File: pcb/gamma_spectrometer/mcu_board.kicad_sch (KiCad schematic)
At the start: 39 parts, among them U301 TL431, U302 STM32G474MET6, U303 W25Q64JVSSIQ, Y301 ABM8G-16.000MHZ-4Y-T3

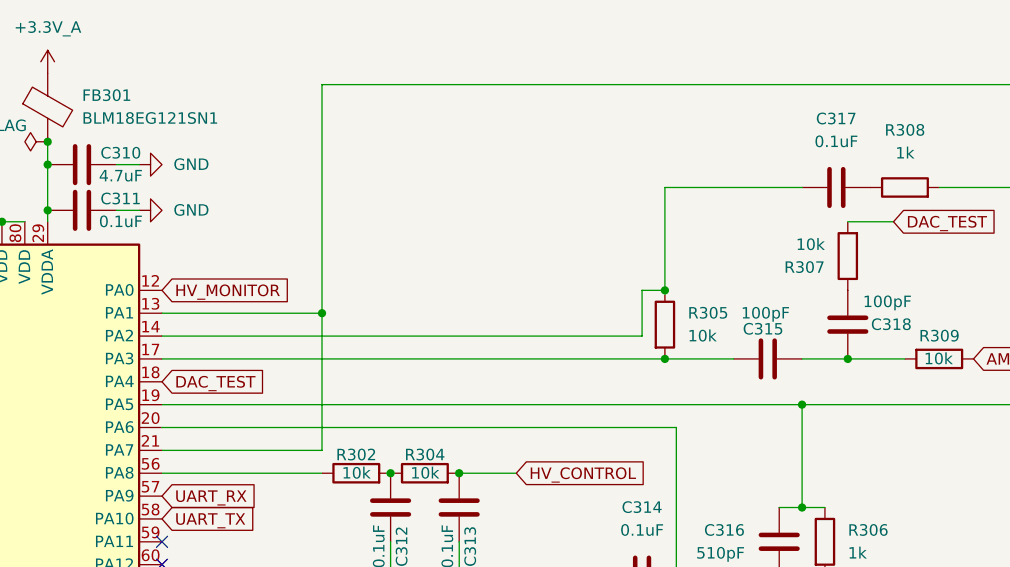
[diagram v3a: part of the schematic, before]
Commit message: pcb: схема MCU + BOM — R314 (R_pz 10k) добавлен пользователем (источник нетлиста)
Согласует репо с уже закоммиченным нетлистом (фикс C2). Схему правил пользователь.

Co-Authored-By: Claude Opus 4.8 <noreply@anthropic.com>
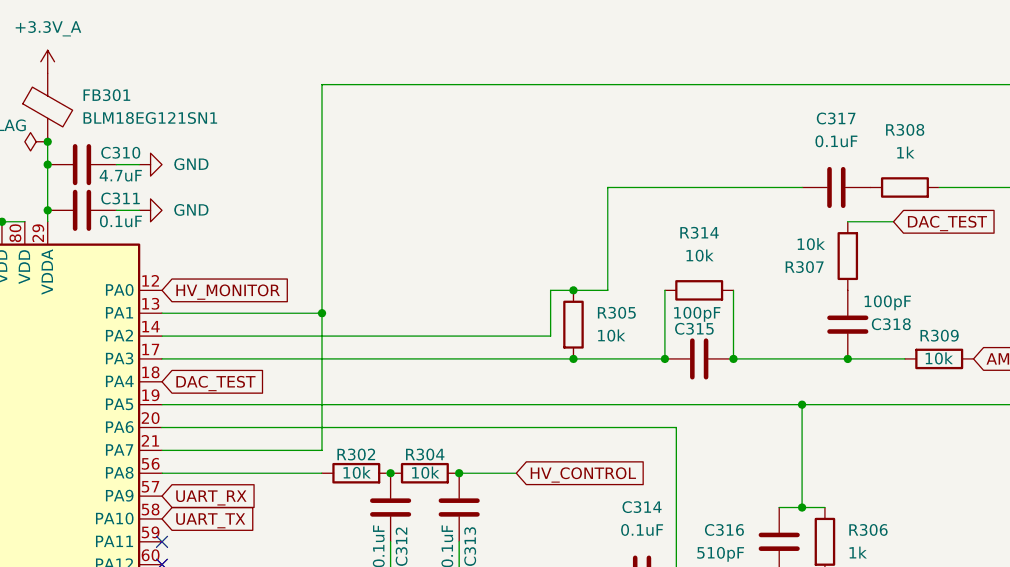
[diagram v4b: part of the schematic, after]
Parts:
- added R314: 10k, Resistor_SMD:R_0603_1608Metric_Pad0.98x0.95mm_HandSolder, symbol Device:R
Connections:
- net at C315.1, C318.1, R309.2: now also R314.2
- net at C315.2, R305.2, U302.17 (PA3): now also R314.1
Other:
- moved on the sheet: C315, R305
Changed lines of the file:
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@@
 	)
 	(junction
-		(at 396.24 173.99)
+		(at 351.79 138.43)
 		(diameter 0)
 		(color 0 0 0 0)
 	)
 	(junction
-		(at 200.66 130.81)
+		(at 396.24 173.99)
 		(diameter 0)
 		(color 0 0 0 0)
 	)
 	(junction
-		(at 344.17 130.81)
+		(at 200.66 130.81)
 		(diameter 0)
 		(color 0 0 0 0)
@@
 	)
 	(junction
+		(at 344.17 138.43)
+		(diameter 0)
+		(color 0 0 0 0)
+	)
+	(junction
 		(at 213.36 130.81)
 		(diameter 0)
@@
 	)
 	(junction
-		(at 344.17 138.43)
+		(at 334.01 138.43)
 		(diameter 0)
 		(color 0 0 0 0)
@@
 	)
 	(junction
+		(at 334.01 130.81)
+		(diameter 0)
+		(color 0 0 0 0)
+	)
+	(junction
 		(at 345.44 162.56)
 		(diameter 0)
@@
 	(wire
 		(pts
-			(xy 344.17 119.38) (xy 344.17 130.81)
+			(xy 337.82 119.38) (xy 337.82 130.81)
 		)
 		(stroke
@@
 	(wire
 		(pts
-			(xy 359.41 138.43) (xy 364.49 138.43)
+			(xy 351.79 138.43) (xy 364.49 138.43)
 		)
 		(stroke
@@
 	(wire
 		(pts
+			(xy 344.17 130.81) (xy 344.17 138.43)
+		)
+		(stroke
+			(width 0)
+			(type default)
+		)
+	)
+	(wire
+		(pts
 			(xy 200.66 128.27) (xy 200.66 130.81)
 		)
@@
 	(wire
 		(pts
+			(xy 334.01 130.81) (xy 337.82 130.81)
+		)
+		(stroke
+			(width 0)
+			(type default)
+		)
+	)
+	(wire
+		(pts
 			(xy 262.89 123.19) (xy 265.43 123.19)
 		)
@@
 	(wire
 		(pts
-			(xy 341.63 135.89) (xy 341.63 130.81)
+			(xy 331.47 135.89) (xy 331.47 130.81)
 		)
 		(stroke
@@
 	(wire
 		(pts
-			(xy 359.41 119.38) (xy 344.17 119.38)
+			(xy 359.41 119.38) (xy 337.82 119.38)
 		)
 		(stroke
@@
 	(wire
 		(pts
+			(xy 351.79 130.81) (xy 351.79 138.43)
+		)
+		(stroke
+			(width 0)
+			(type default)
+		)
+	)
+	(wire
+		(pts
 			(xy 260.35 123.19) (xy 262.89 123.19)
 		)
@@
 	(wire
 		(pts
-			(xy 306.07 148.59) (xy 288.29 148.59)
+			(xy 334.01 138.43) (xy 344.17 138.43)
 		)
 		(stroke
@@
 	(wire
 		(pts
-			(xy 341.63 130.81) (xy 344.17 130.81)
+			(xy 306.07 148.59) (xy 288.29 148.59)
 		)
 		(stroke
@@
 	(wire
 		(pts
-			(xy 265.43 120.65) (xy 265.43 123.19)
+			(xy 331.47 130.81) (xy 334.01 130.81)
 		)
 		(stroke
@@
 	(wire
 		(pts
-			(xy 359.41 143.51) (xy 359.41 154.94)
+			(xy 265.43 120.65) (xy 265.43 123.19)
 		)
 		(stroke
@@
 	(wire
 		(pts
-			(xy 288.29 138.43) (xy 344.17 138.43)
+			(xy 359.41 143.51) (xy 359.41 154.94)
 		)
 		(stroke
@@
 	(wire
 		(pts
-			(xy 288.29 135.89) (xy 341.63 135.89)
+			(xy 288.29 138.43) (xy 334.01 138.43)
 		)
 		(stroke
@@
 	(wire
 		(pts
-			(xy 321.31 151.13) (xy 327.66 151.13)
+			(xy 288.29 135.89) (xy 331.47 135.89)
 		)
 		(stroke
@@
 	(wire
 		(pts
-			(xy 401.32 66.04) (xy 396.24 66.04)
+			(xy 321.31 151.13) (xy 327.66 151.13)
 		)
 		(stroke
@@
 	(wire
 		(pts
-			(xy 247.65 143.51) (xy 243.84 143.51)
+			(xy 401.32 66.04) (xy 396.24 66.04)
 		)
 		(stroke
@@
 	(wire
 		(pts
-			(xy 344.17 138.43) (xy 351.79 138.43)
+			(xy 247.65 143.51) (xy 243.84 143.51)
 		)
 		(stroke
@@
 	(symbol
 		(lib_id "Device:C")
-		(at 355.6 138.43 270)
+		(at 347.98 138.43 270)
 		(unit 1)
 		(exclude_from_sim no)
@@
 		(dnp no)
 		(property "Reference" "C315"
-			(at 355.092 135.128 90)
+			(at 347.472 135.128 90)
 			(effects
 				(font
@@
 		)
 		(property "Value" "100pF"
-			(at 355.346 133.35 90)
+			(at 347.726 133.35 90)
 			(effects
 				(font
@@
 		)
 		(property "Footprint" "Capacitor_SMD:C_0603_1608Metric_Pad1.08x0.95mm_HandSolder"
-			(at 351.79 139.3952 0)
+			(at 344.17 139.3952 0)
 			(effects
 				(font
@@
 		)
 		(property "Datasheet" "~"
-			(at 355.6 138.43 0)
+			(at 347.98 138.43 0)
 			(effects
 				(font
@@
 		)
 		(property "Description" "Unpolarized capacitor"
-			(at 355.6 138.43 0)
+			(at 347.98 138.43 0)
 			(effects
 				(font
@@
 		)
 		(property "KLC_S3.3" ""
-			(at 355.6 138.43 90)
+			(at 347.98 138.43 90)
 			(effects
 				(font
@@
 		)
 		(property "KLC_S4.1" ""
-			(at 355.6 138.43 90)
+			(at 347.98 138.43 90)
 			(effects
 				(font
@@
 		)
 		(property "PN" "CC0603JRNPO9BN101"
-			(at 355.6 138.43 90)
+			(at 347.98 138.43 90)
 			(effects
 				(font
@@
 		)
 		(property "Ссылка на покупку " "https://www.electronshik.ru/item/YAG/CC0603JRNPO9BN101"
-			(at 355.6 138.43 90)
+			(at 347.98 138.43 90)
 			(effects
 				(font
@@
 	)
 	(symbol
+		(lib_id "Device:R")
+		(at 347.98 130.81 90)
+		(unit 1)
+		(exclude_from_sim no)
+		(in_bom yes)
+		(on_board yes)
+		(dnp no)
+		(fields_autoplaced yes)
+		(property "Reference" "R314"
+			(at 347.98 124.46 90)
+			(effects
+				(font
+					(size 1.27 1.27)
+				)
+			)
+		)
+		(property "Value" "10k"
+			(at 347.98 127 90)
+			(effects
+				(font
+					(size 1.27 1.27)
+				)
+			)
+		)
+		(property "Footprint" "Resistor_SMD:R_0603_1608Metric_Pad0.98x0.95mm_HandSolder"
+			(at 347.98 132.588 90)
+			(effects
+				(font
+					(size 1.27 1.27)
+				)
+				(hide yes)
+			)
+		)
+		(property "Datasheet" "~"
+			(at 347.98 130.81 0)
+			(effects
+				(font
+					(size 1.27 1.27)
+				)
+				(hide yes)
+			)
+		)
+		(property "Description" "Resistor"
+			(at 347.98 130.81 0)
+			(effects
+				(font
+					(size 1.27 1.27)
+				)
+				(hide yes)
+			)
+		)
+		(property "PN" "RC0603FR-0710KL"
+			(at 347.98 130.81 90)
+			(effects
+				(font
+					(size 1.27 1.27)
+				)
+				(hide yes)
+			)
+		)
+		(property "Ссылка на покупку " "https://www.electronshik.ru/item/YAG/RC0603FR-0710KL"
+			(at 347.98 130.81 90)
+			(effects
+				(font
+					(size 1.27 1.27)
+				)
+				(hide yes)
+			)
+		)
+		(pin "1"
+		)
+		(pin "2"
+		)
+		(instances
+			(project ""
+				(path "/9de23c55-b97f-4e07-9aa5-29ce30f3c480/0e491218-e2a9-4640-b27e-9c4e6f92e006"
+					(reference "R314")
+					(unit 1)
+				)
+			)
+		)
+	)
+	(symbol
 		(lib_id "power:GND")
 		(at 402.59 115.57 0)
@@
 	(symbol
 		(lib_id "Device:R")
-		(at 344.17 134.62 0)
+		(at 334.01 134.62 0)
 		(unit 1)
 		(exclude_from_sim no)
@@
 		(fields_autoplaced yes)
 		(property "Reference" "R305"
-			(at 346.71 133.3499 0)
+			(at 336.55 133.3499 0)
 			(effects
 				(font
@@
 		)
 		(property "Value" "10k"
-			(at 346.71 135.8899 0)
+			(at 336.55 135.8899 0)
 			(effects
 				(font
@@
 		)
 		(property "Footprint" "Resistor_SMD:R_0603_1608Metric_Pad0.98x0.95mm_HandSolder"
-			(at 342.392 134.62 90)
+			(at 332.232 134.62 90)
 			(effects
 				(font
@@
 		)
 		(property "Datasheet" "~"
-			(at 344.17 134.62 0)
+			(at 334.01 134.62 0)
 			(effects
 				(font
@@
 		)
 		(property "Description" "Resistor"
-			(at 344.17 134.62 0)
+			(at 334.01 134.62 0)
 			(effects
 				(font
@@
 		)
 		(property "KLC_S3.3" ""
-			(at 344.17 134.62 0)
+			(at 334.01 134.62 0)
 			(effects
 				(font
@@
 		)
 		(property "KLC_S4.1" ""
-			(at 344.17 134.62 0)
+			(at 334.01 134.62 0)
 			(effects
 				(font
@@
 		)
 		(property "PN" "RC0603FR-0710KL"
-			(at 344.17 134.62 0)
+			(at 334.01 134.62 0)
 			(effects
 				(font
@@
 		)
 		(property "Ссылка на покупку " "https://www.electronshik.ru/item/YAG/RC0603FR-0710KL"
-			(at 344.17 134.62 0)
+			(at 334.01 134.62 0)
 			(effects
 				(font

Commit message: fix: полярность тракта, опора REF35250, DRC по электрике в ноль
ПОЛЯРНОСТЬ (главное). Анод ФЭУ забирает условный ток => выход TIA идёт
вверх => импульс на АЦП положительный. В доках и прошивке была обратная
конвенция, выросшая из sim2_shaper.cir, где источник тока анода развёрнут
(`I_pmt 0 anode` вместо `I_pmt anode 0`); sim_divider_complete.cir всё это
время делал верно — две деки противоречили друг другу.

Последствия при старых смещениях (sim_polarity_headroom.cir, реальная
модель ADA4817): OPAMP1 уходил вниз до -1.09 В при VOLSAT 100 мВ (клиппинг
с ~1.2 МэВ), АЦП вверх до 3.99 В при VREF+ 2.495 (обрезка с ~0.70 МэВ).
Прибор мерил бы до 700 кэВ вместо 3.5 МэВ.

Исправление — два резистора, железо не переделывается:
  R313 2.0к -> 14.7к   V_A 0.490 -> 1.602 В
  R311 5.9к -> 909     V_PB0 0.529 -> 0.099 В, базовая линия АЦП -> 0.408 В
Запасы на потолке 3.5 МэВ (sim_bias_fixed.cir): OPAMP1 0.575..2.515,
OPAMP2 1.580..2.082, АЦП 0.308..2.276 (до VREF+ +0.224 В).
Попутно вскрыто: выход OPAMP1 сидит на 1.5*V_A, а не на V_A — R314 (фикс C2)
создаёт путь по постоянному току в обход C315. Нигде не было записано.
В прошивке остаётся сделать `amplitude = sample - baseline`.

ОПОРА. TL431DBZ -> REF35250QDBVR (SOT-23-6) по итогам ревью инженера:
параметрический шунт заменён последовательной опорой. 12 ppm/°C вместо 50
(у клона YOUTAI до 300), точность ±0.05%. Дрейф калибровки на ±30 °C:
0.9% -> 0.036%. R301 удалён, C303 100нФ -> 1мкФ (обязательный выходной),
добавлен C322 1мкФ на вывод NR. Правило шпаргалки №9 (ток шунта) для U301
больше не применимо; U202 на ВВ-плате остаётся TL431.
⚠ REF35205, который он назвал — это 2.048 В, не подходит (пик 2.118 В).

DRC. По электрике ноль нарушений: clearance, track_dangling, via_dangling,
holes_co_located, starved_thermal — все пусты. Всего 774 -> 402, остаток
целиком шелкография и courtyard.
- 25 GND-падов переведены на сплошное соединение с зоной (стойки, развязка,
  кварц, земля MAX1847, выход опоры)
- экран USB-C заземлён: J101 пер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
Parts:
- removed R301: R330, Resistor_SMD:R_0603_1608Metric_Pad0.98x0.95mm_HandSolder, symbol Device:R
- removed U301: TL431, Package_TO_SOT_SMD:SOT-23, symbol Reference_Voltage:TL431DBZ
- added C322: 1uF, Capacitor_SMD:C_0805_2012Metric_Pad1.18x1.45mm_HandSolder, symbol Device:C
- added U301: REF35250QDBVR, Package_TO_SOT_SMD:SOT-23-6, symbol Reference_Voltage:REF35250QDBVR
- C303: value 0.1uF -> 1uF; footprint Capacitor_SMD:C_0603_1608Metric_Pad1.08x0.95mm_HandSolder -> Capacitor_SMD:C_0805_2012Metric_Pad1.18x1.45mm_HandSolder; PN CC0603JRX7R9BB104 -> CC0805JKX7R9BB105; Ссылка на покупку  https://www.electronshik.ru/item/YAG/CC0603JRX7R9BB104 -> https://www.electronshik.ru/item/YAG/CC0805JKX7R9BB105
- R311: value 5.9k -> 909R; PN RC0603FR-075K9L -> RC0603FR-07909RL; Ссылка на покупку  https://www.electronshik.ru/item/YAG/RC0603FR-075K9L -> https://www.electronshik.ru/item/YAG/RC0603FR-07909RL
- R313: value 2k -> 14.7k; PN RC0603FR-072KL -> RC0603FR-0714K7L; Ссылка на покупку  https://www.electronshik.ru/item/YAG/RC0603FR-072KL -> https://www.electronshik.ru/item/YAG/RC0603FR-0714K7L
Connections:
- net +3.3V_A: now also U301.3 (EN), U301.4 (VIN)
- net GND: now also C322.2, U301.1 (GND), U301.2 (GND)
- net at C303.2, R303.1, R310.1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: now also U301.6 (VREF)
- new net: C322.1, U301.5 (NR)

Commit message: pcb: земля МК подключена, C320 удалён, C314/C317 → 1 мкФ, SWD-пятаки убраны
Плата МК:
- все GND-выводы U302 подключены (15, 27/VSSA, 40, 50 висели);
  зона GND на F.Cu: зазор 0.5 → 0.25 мм, зазор термобарьера → 0.2 мм;
  GND-виа 41 → 97. Остаётся: выводы 50 и 61 на одной спице (starved_thermal).
- TP_SWD301 удалён: прошивка — проводами к выводам 63/64/7 U302.

Схема МК (ревью REVIEW_critic_2026-09-15, находки 1.1 и 1.3, вариант V2):
- C320 удалён (100 нФ на PB0 делил сигнал ×0.5 вместе с C314);
- C314, C317: 100 нФ → 1 мкФ (CC0603JRX7R7BB105), τ связей ~1 мс.

USB-плата: J101 на проектной копии футпринта USB-C (экран на GND).

Co-Authored-By: Claude Opus 5 (1M context) <noreply@anthropic.com>
Claude-Session: https://claude.ai/code/session_018uEKxzknn1WsQbGcTkkQF5
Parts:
- removed C320: 0.1uF, Capacitor_SMD:C_0603_1608Metric_Pad1.08x0.95mm_HandSolder, symbol Device:C
- C314, C317: value 0.1uF -> 1uF; PN CC0603JRX7R9BB104 -> CC0603JRX7R7BB105; Ссылка на покупку  https://www.electronshik.ru/item/YAG/CC0603JRX7R9BB104 -> https://www.electronshik.ru/item/YAG/CC0603JRX7R7BB105
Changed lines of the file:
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@@
 			)
 		)
-		(property "Value" "0.1uF"
+		(property "Value" "1uF"
 			(at 341.63 157.48 90)
 			(effects
@@
 			)
 		)
-		(property "PN" "CC0603JRX7R9BB104"
+		(property "PN" " CC0603JRX7R7BB105"
 			(at 341.63 162.56 90)
 			(effects
@@
 			)
 		)
-		(property "Ссылка на покупку " "https://www.electronshik.ru/item/YAG/CC0603JRX7R9BB104"
+		(property "Ссылка на покупку " "https://www.electronshik.ru/item/YAG/CC0603JRX7R7BB105"
 			(at 341.63 162.56 90)
 			(effects
@@
 	)
 	(symbol
-		(lib_id "power:GND")
-		(at 403.86 173.99 90)
-		(mirror x)
-		(unit 1)
-		(exclude_from_sim no)
-		(in_bom yes)
-		(on_board yes)
-		(dnp no)
-		(fields_autoplaced yes)
-		(property "Reference" "#PWR0320"
-			(at 410.21 173.99 0)
-			(effects
-				(font
-					(size 1.27 1.27)
-				)
-				(hide yes)
-			)
-		)
-		(property "Value" "GND"
-			(at 408.94 173.99 0)
-			(effects
-				(font
-					(size 1.27 1.27)
-				)
-			)
-		)
-		(property "Footprint" ""
-			(at 403.86 173.99 0)
-			(effects
-				(font
-					(size 1.27 1.27)
-				)
-				(hide yes)
-			)
-		)
-		(property "Datasheet" ""
-			(at 403.86 173.99 0)
-			(effects
-				(font
-					(size 1.27 1.27)
-				)
-				(hide yes)
-			)
-		)
-		(property "Description" "Power symbol creates a global label with name \"GND\" , ground"
-			(at 403.86 173.99 0)
-			(effects
-				(font
-					(size 1.27 1.27)
-				)
-				(hide yes)
-			)
-		)
-		(pin "1"
-		)
-		(instances
-			(project "gamma_spectrometer"
-				(path "/9de23c55-b97f-4e07-9aa5-29ce30f3c480/0e491218-e2a9-4640-b27e-9c4e6f92e006"
-					(reference "#PWR0320")
-					(unit 1)
-				)
-			)
-		)
-	)
-	(symbol
 		(lib_id "Device:C")
 		(at 198.12 123.19 0)
@@
 			)
 		)
-		(property "Value" "0.1uF"
+		(property "Value" "1uF"
 			(at 363.22 114.3 90)
 			(effects
@@
 			)
 		)
-		(property "PN" "CC0603JRX7R9BB104"
+		(property "PN" "CC0603JRX7R7BB105"
 			(at 363.22 119.38 90)
 			(effects
@@
 			)
 		)
-		(property "Ссылка на покупку " "https://www.electronshik.ru/item/YAG/CC0603JRX7R9BB104"
+		(property "Ссылка на покупку " "https://www.electronshik.ru/item/YAG/CC0603JRX7R7BB105"
 			(at 363.22 119.38 90)
 			(effects
@@
 					(unit 1)
 				)
-			)
-		)
-	)
-	(symbol
-		(lib_id "Device:C")
-		(at 400.05 173.99 90)
-		(mirror x)
-		(unit 1)
-		(exclude_from_sim no)
-		(in_bom yes)
-		(on_board yes)
-		(dnp no)
-		(property "Reference" "C320"
-			(at 398.7799 177.8 0)
-			(effects
-				(font
-					(size 1.27 1.27)
-				)
-				(justify left)
-			)
-		)
-		(property "Value" "0.1uF"
-			(at 401.3199 177.8 0)
-			(effects
-				(font
-					(size 1.27 1.27)
-				)
-				(justify left)
-			)
-		)
-		(property "Footprint" "Capacitor_SMD:C_0603_1608Metric_Pad1.08x0.95mm_HandSolder"
-			(at 403.86 174.9552 0)
-			(effects
-				(font
-					(size 1.27 1.27)
-				)
-				(hide yes)
-			)
-		)
-		(property "Datasheet" "~"
-			(at 400.05 173.99 0)
-			(effects
-				(font
-					(size 1.27 1.27)
-				)
-				(hide yes)
-			)
-		)
-		(property "Description" "Unpolarized capacitor"
-			(at 400.05 173.99 0)
-			(effects
-				(font
-					(size 1.27 1.27)
-				)
-				(hide yes)
-			)
-		)
-		(property "KLC_S3.3" ""
-			(at 400.05 173.99 0)
-			(effects
-				(font
-					(size 1.27 1.27)
-				)
-				(hide yes)
-			)
-		)
-		(property "KLC_S4.1" ""
-			(at 400.05 173.99 0)
-			(effects
-				(font
-					(size 1.27 1.27)
-				)
-				(hide yes)
-			)
-		)
-		(property "PN" "CC0603JRX7R9BB104"
-			(at 400.05 173.99 0)
-			(effects
-				(font
-					(size 1.27 1.27)
-				)
-				(hide yes)
-			)
-		)
-		(property "Ссылка на покупку " "https://www.electronshik.ru/item/YAG/CC0603JRX7R9BB104"
-			(at 400.05 173.99 0)
-			(effects
-				(font
-					(size 1.27 1.27)
-				)
-				(hide yes)
-			)
-		)
-		(pin "1"
-		)
-		(pin "2"
-		)
-		(instances
-			(project ""
-				(path "/9de23c55-b97f-4e07-9aa5-29ce30f3c480/0e491218-e2a9-4640-b27e-9c4e6f92e006"
-					(reference "C320")
-					(unit 1)
-				)

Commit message: sch: C314 — убран пробел в начале PN
Co-Authored-By: Claude Opus 5 (1M context) <noreply@anthropic.com>
Claude-Session: https://claude.ai/code/session_018uEKxzknn1WsQbGcTkkQF5
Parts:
- C314: PN CC0603JRX7R7BB105 -> CC0603JRX7R7BB105
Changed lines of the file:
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@@
 			)
 		)
-		(property "PN" " CC0603JRX7R7BB105"
+		(property "PN" "CC0603JRX7R7BB105"
 			(at 341.63 162.56 90)
 			(effects
